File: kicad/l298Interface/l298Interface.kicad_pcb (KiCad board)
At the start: 2 copper layers, 13.5 x 30 mm, 2 parts

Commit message: added links to machine tool movies
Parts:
- added REF**: TerminalBlock_Phoenix_MKDS-1,5-3-5.08_1x03_P5.08mm_Horizont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, TerminalBlock_Phoenix:TerminalBlock_Phoenix_MKDS-1,5-3-5.08_1x03_P5.08mm_Horizontal, F.Cu at (114.0, 81.3)
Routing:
- net (no net): track 54.1 -> 64.2 mm
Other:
- board size 13.5 x 30 mm -> 13.5 x 49 mm

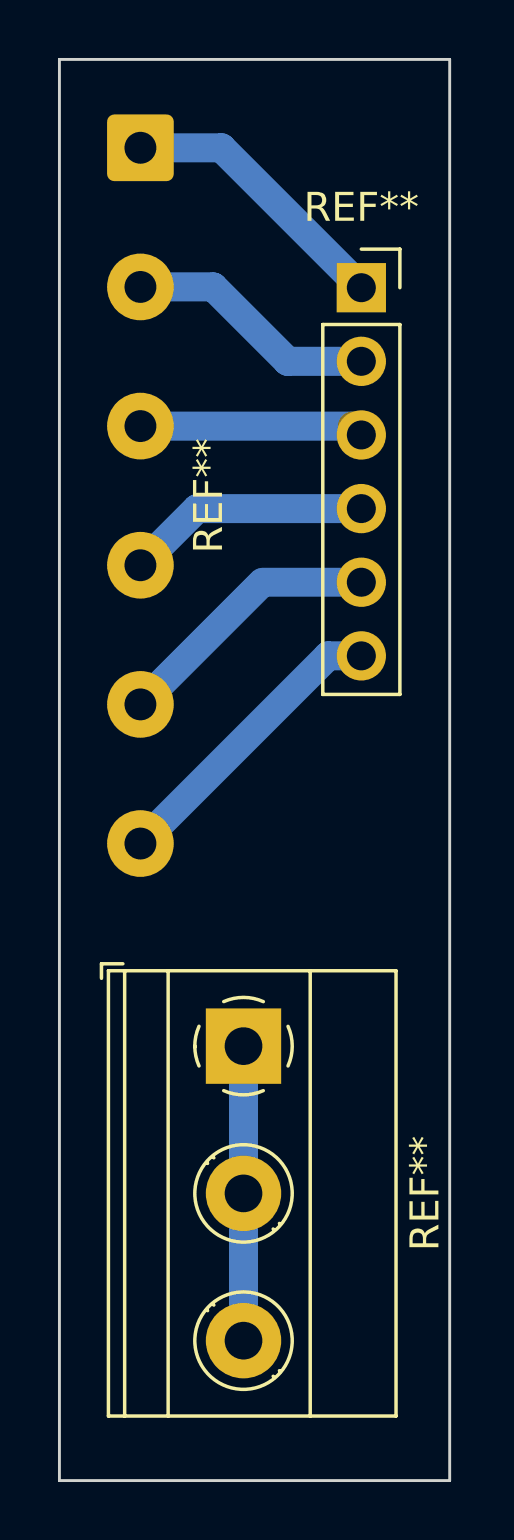
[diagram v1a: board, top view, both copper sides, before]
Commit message: finished hobby rc and motor controller shield
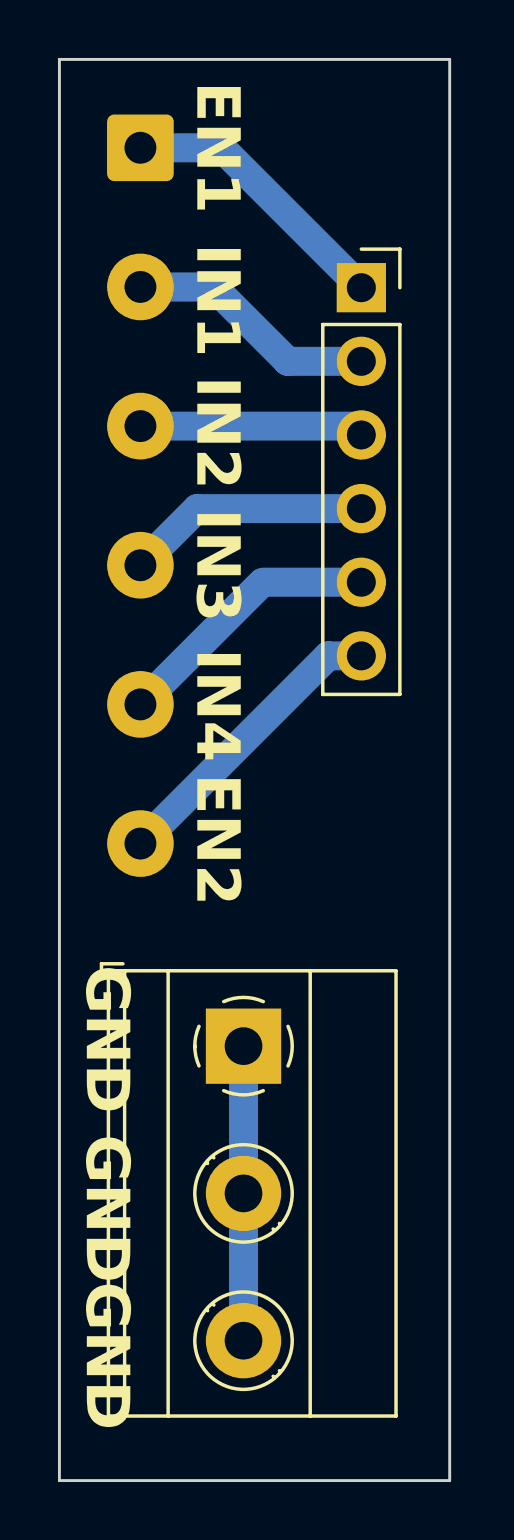
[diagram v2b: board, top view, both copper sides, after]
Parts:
- renumbered REF** to ?, REF** to GND
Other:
- board text added: "EN1"
- board text added: "EN2"
- board text added: "GND"
- board text added: "IN1"
- board text added: "IN2"
- board text added: "IN3"
- board text added: "IN4"
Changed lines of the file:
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@@
     (pad_to_mask_clearance 0)
     (pcbplotparams
-      (layerselection 0x00010f0_ffffffff)
+      (layerselection 0x00010fc_ffffffff)
       (plot_on_all_layers_selection 0x0000000_00000000)
       (disableapertmacros false)
@@
     (tags "Through hole socket strip THT 1x06 2.54mm single row")
     (attr through_hole)
-    (fp_text reference "REF**" (at 0 -2.77) (layer "F.SilkS")
+    (fp_text reference "REF**" (at 0 -2.77) (layer "F.SilkS") hide
         (effects (font (size 1 1) (thickness 0.15)))
     )
@@
     (tags "THT Terminal Block Phoenix MKDS-1,5-3-5.08 pitch 5.08mm size 15.2x9.8mm^2 drill 1.3mm pad 2.6mm")
     (attr through_hole)
-    (fp_text reference "REF**" (at 5.08 -6.26 90) (layer "F.SilkS")
+    (fp_text reference "GND" (at 5.08 -6.26 90) (layer "F.SilkS") hide
         (effects (font (size 1 1) (thickness 0.15)))
     )
@@
     (tags "connector wire 0.5sqmm")
     (attr exclude_from_pos_files exclude_from_bom)
-    (fp_text reference "REF**" (at 12 -2.35 90) (layer "F.SilkS")
+    (fp_text reference "" (at 12 -2.35 90) (layer "F.SilkS") hide
         (effects (font (size 1 1) (thickness 0.15)))
     )
@@
   (gr_rect (start 107.696 47.244) (end 121.158 96.266)
     (stroke (width 0.1) (type default)) (fill none) (layer "Edge.Cuts"))
-  (segment (start 117.804 59.892) (end 118.11 60.198) (width 1) (layer "F.Cu") (net 0))
+  (gr_text "EN1" (at 112.268 48.006 -90) (layer "F.SilkS")
+    (effects (font (size 1.5 1.5) (thickness 0.3) bold) (justify left bottom))
+  )
+  (gr_text "IN3" (at 112.268 62.738 -90) (layer "F.SilkS")
+    (effects (font (size 1.5 1.5) (thickness 0.3) bold) (justify left bottom))
+  )
+  (gr_text "IN1" (at 112.268 53.594 -90) (layer "F.SilkS")
+    (effects (font (size 1.5 1.5) (thickness 0.3) bold) (justify left bottom))
+  )
+  (gr_text "IN4\n" (at 112.268 67.564 270) (layer "F.SilkS")
+    (effects (font (size 1.5 1.5) (thickness 0.3) bold) (justify left bottom))
+  )
+  (gr_text "IN2" (at 112.268 58.166 -90) (layer "F.SilkS")
+    (effects (font (size 1.5 1.5) (thickness 0.3) bold) (justify left bottom))
+  )
+  (gr_text "GND" (at 108.458 84.328 -90) (layer "F.SilkS")
+    (effects (font (size 1.5 1.5) (thickness 0.3) bold) (justify left bottom))
+  )
+  (gr_text "EN2" (at 112.268 71.882 -90) (layer "F.SilkS")
+    (effects (font (size 1.5 1.5) (thickness 0.3) bold) (justify left bottom))
+  )
+  (gr_text "GND" (at 108.458 78.486 -90) (layer "F.SilkS")
+    (effects (font (size 1.5 1.5) (thickness 0.3) bold) (justify left bottom))
+  )
+  (gr_text "GND" (at 108.458 89.408 -90) (layer "F.SilkS")
+    (effects (font (size 1.5 1.5) (thickness 0.3) bold) (justify left bottom))
+  )
+  (gr_text_box "l298 Interface Michael Shiloh GPLv3 "
+    (start 121.6152 46.99) (end 105.9688 77.978) (angle -90) (layer "F.SilkS")
+      (effects (font (size 1 1) (thickness 0.2) bold) (justify left top))
+    (stroke (width 0.2) (type solid))  )
   (segment (start 110.49 59.892) (end 117.804 59.892) (width 1) (layer "B.Cu") (net 0))
   (segment (start 118.11 65.278) (end 114.704 65.278) (width 1) (layer "B.Cu") (net 0))
